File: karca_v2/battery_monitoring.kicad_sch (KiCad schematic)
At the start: 14 parts, among them U33 INA180A2, U34 MCP3204, U35 NUP4202, U36 TLV9301xDBV

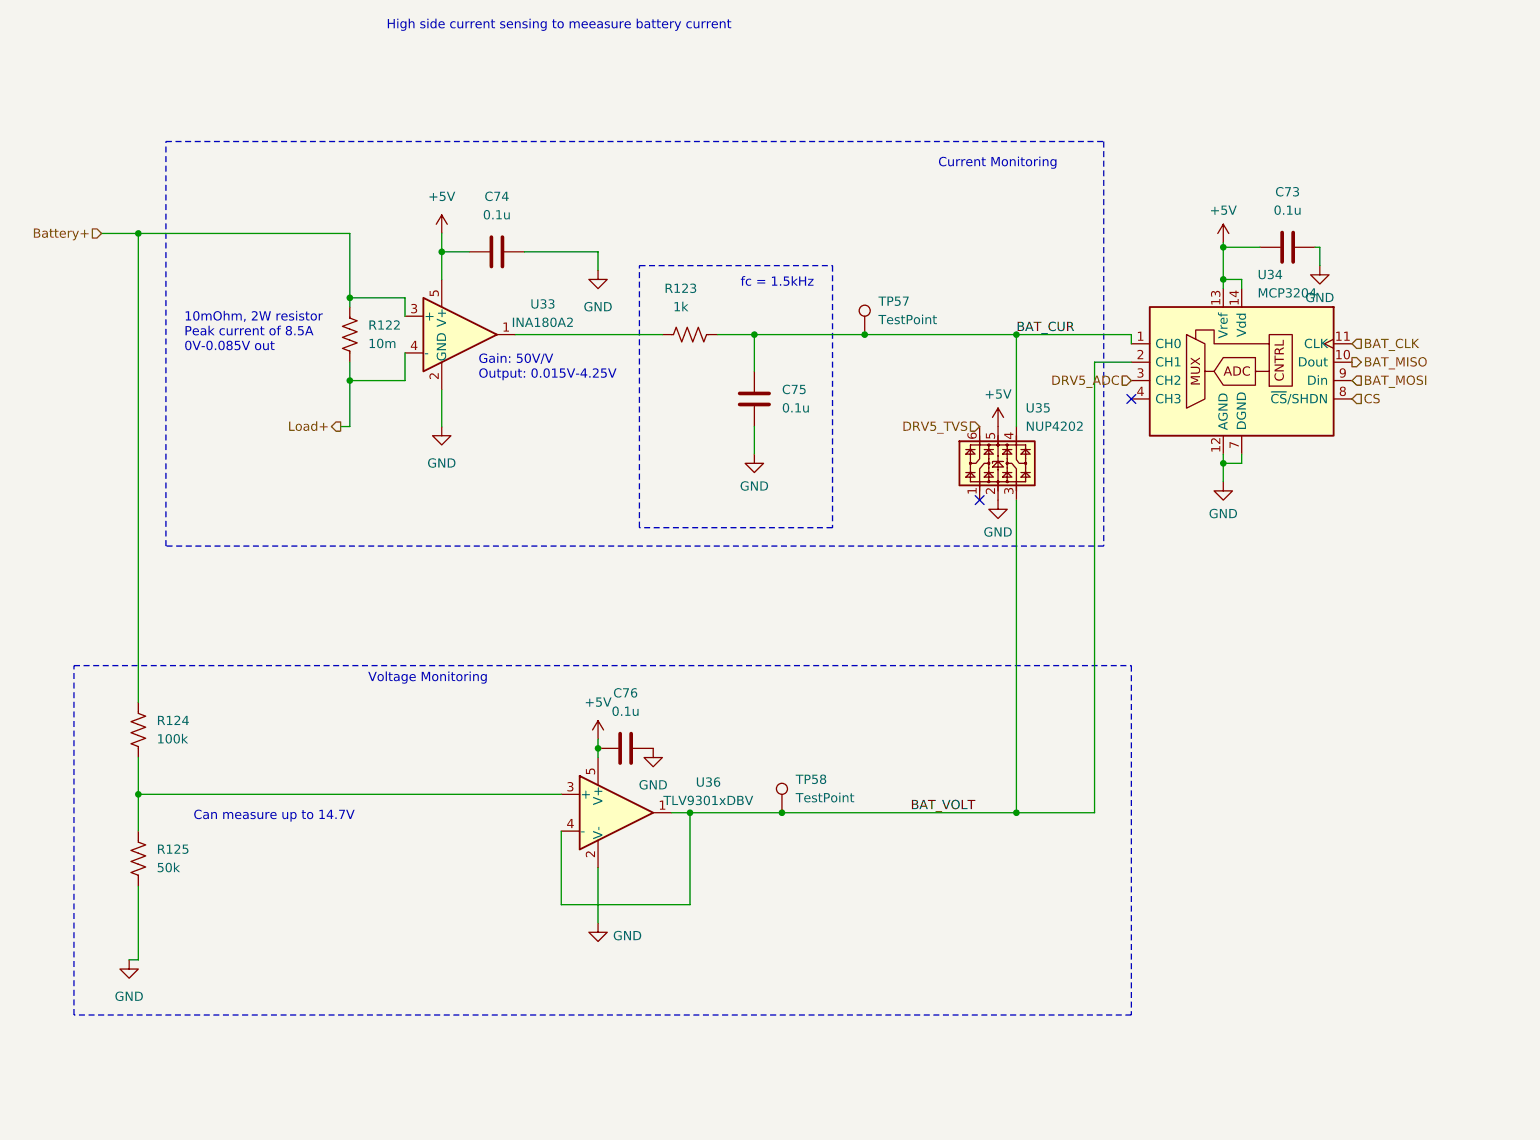
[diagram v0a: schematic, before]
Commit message: reorganized ADCs
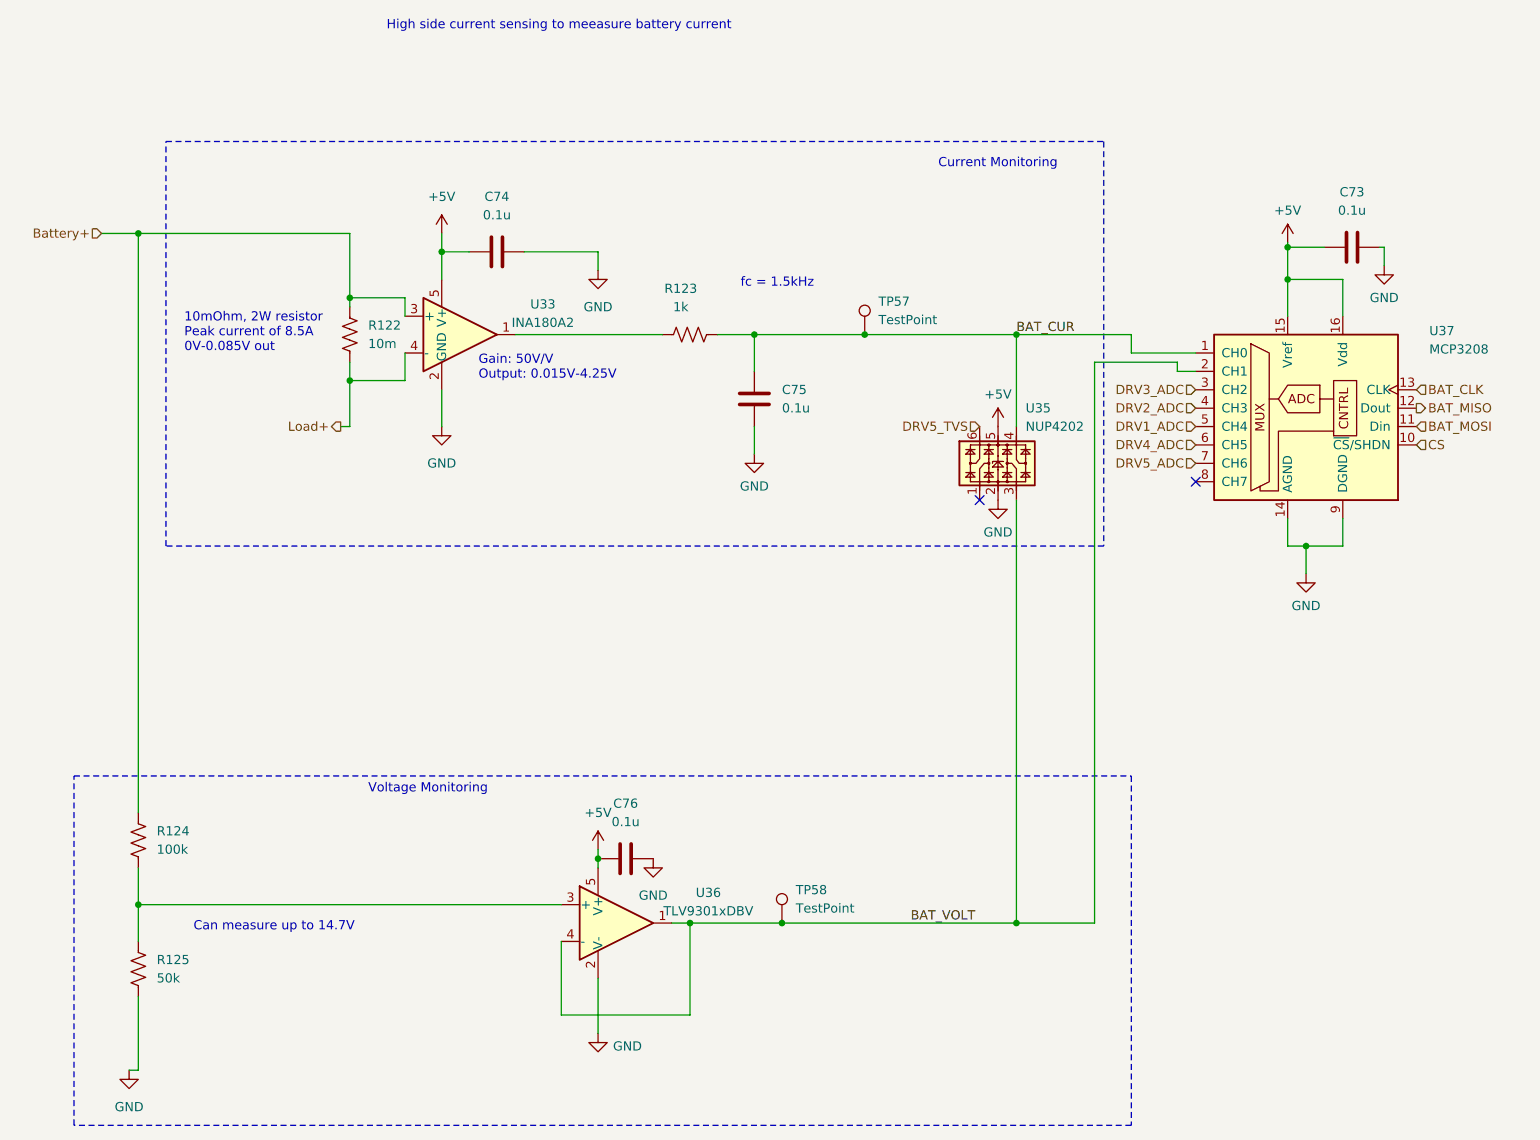
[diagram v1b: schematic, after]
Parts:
- removed U34: MCP3204, Package_SO:SO-14_3.9x8.65mm_P1.27mm, symbol Analog_ADC:MCP3204
- added U37: MCP3208, Package_SO:SOIC-16_3.9x9.9mm_P1.27mm, symbol Analog_ADC:MCP3208
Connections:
- net +5V: now also U37.15 (Vref), U37.16 (Vdd)
- net BAT_CLK: now also U37.13 (CLK)
- net BAT_CUR: now also U37.1 (CH0)
- net BAT_MISO: now also U37.12 (Dout)
- net BAT_MOSI: now also U37.11 (Din)
- net BAT_VOLT: now also U37.2 (CH1)
- net CS: now also U37.10 (~{CS}/SHDN)
- net DRV5_ADC: now also U37.7 (CH6)
- net GND: now also U37.14 (AGND), U37.9 (DGND)
- new net DRV1_ADC: U37.5 (CH4)
- new net DRV2_ADC: U37.4 (CH3)
- new net DRV3_ADC: U37.3 (CH2)
- new net DRV4_ADC: U37.6 (CH5)
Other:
- moved on the sheet: C73, C76, R124, R125, TP58, U36

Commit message: finished schematic for v2.1
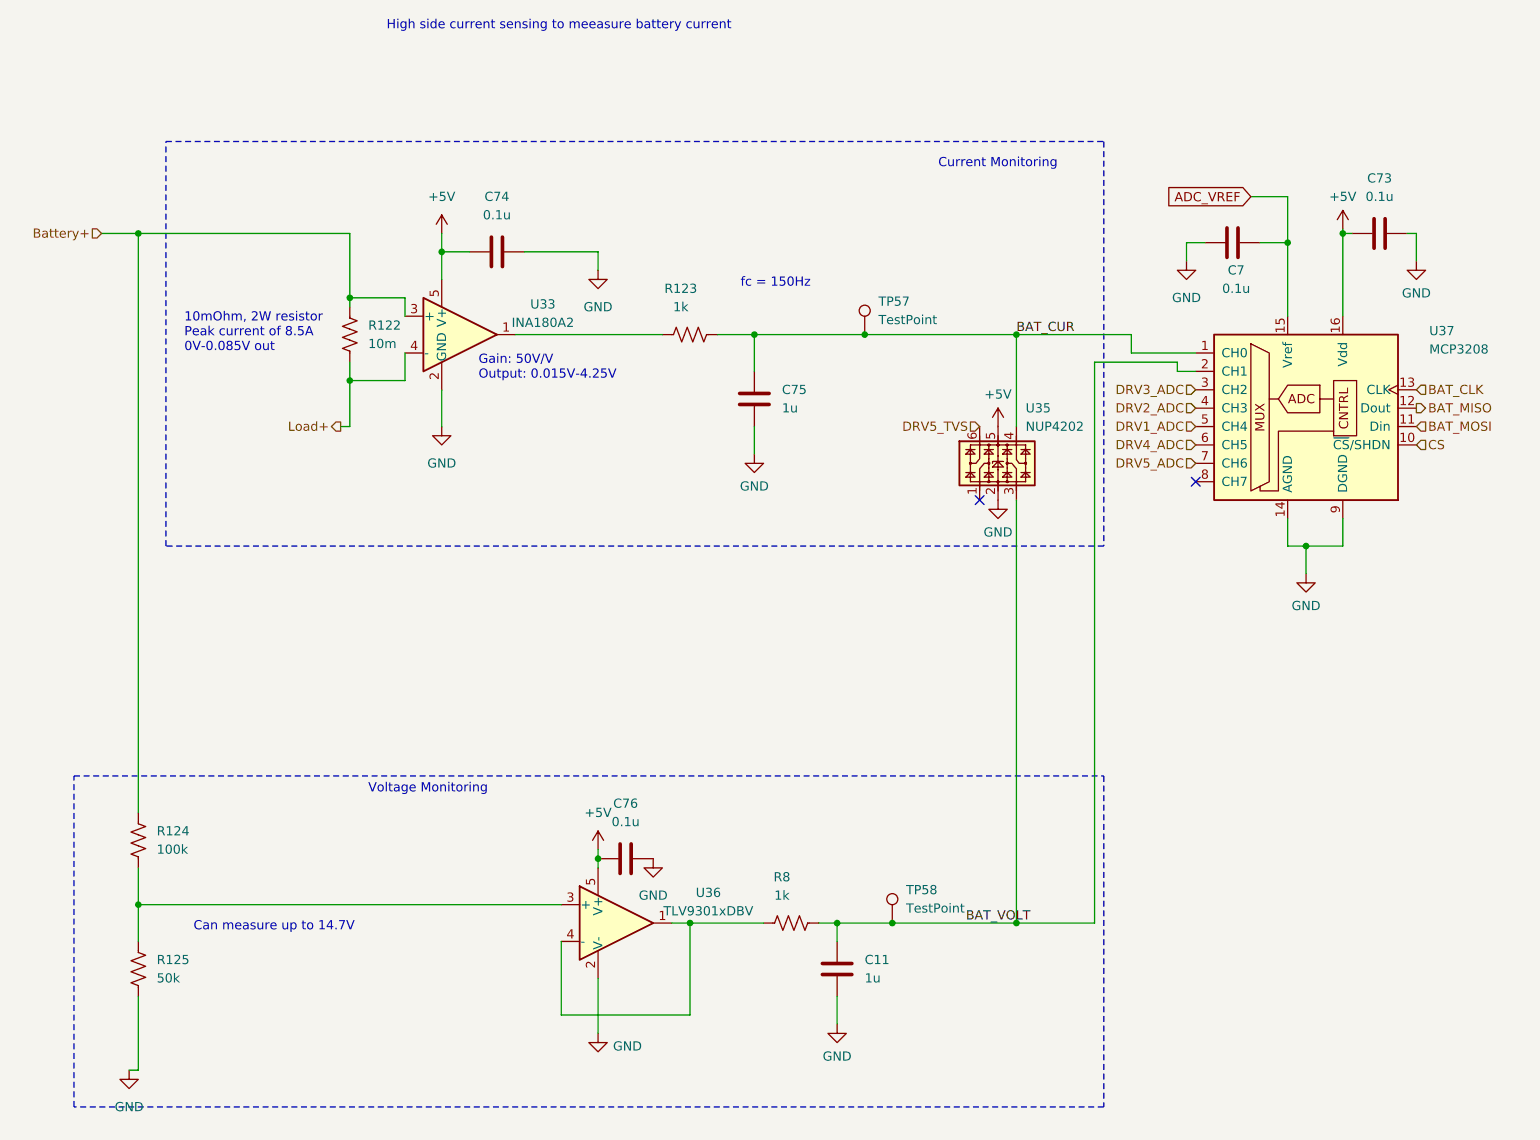
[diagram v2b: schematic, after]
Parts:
- added C11: 1u, Capacitor_SMD:C_1206_3216Metric, symbol Device:C
- added C7: 0.1u, Capacitor_SMD:C_1206_3216Metric, symbol Device:C
- added R8: 1k, Resistor_SMD:R_1206_3216Metric, symbol Device:R_US
- C75: value 0.1u -> 1u
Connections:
- net +5V: no longer U37.15 (Vref)
- net BAT_VOLT: now also C11.2, R8.2; no longer U36.1, U36.4 (-)
- net GND: now also C11.1, C7.1
- new net: R8.1, U36.1, U36.4 (-)
- new net ADC_VREF: C7.2, U37.15 (Vref)
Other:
- note added: "fc = 150Hz"
- note removed: "fc = 1.5kHz"
- moved on the sheet: C73, TP58

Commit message: swapped adcs
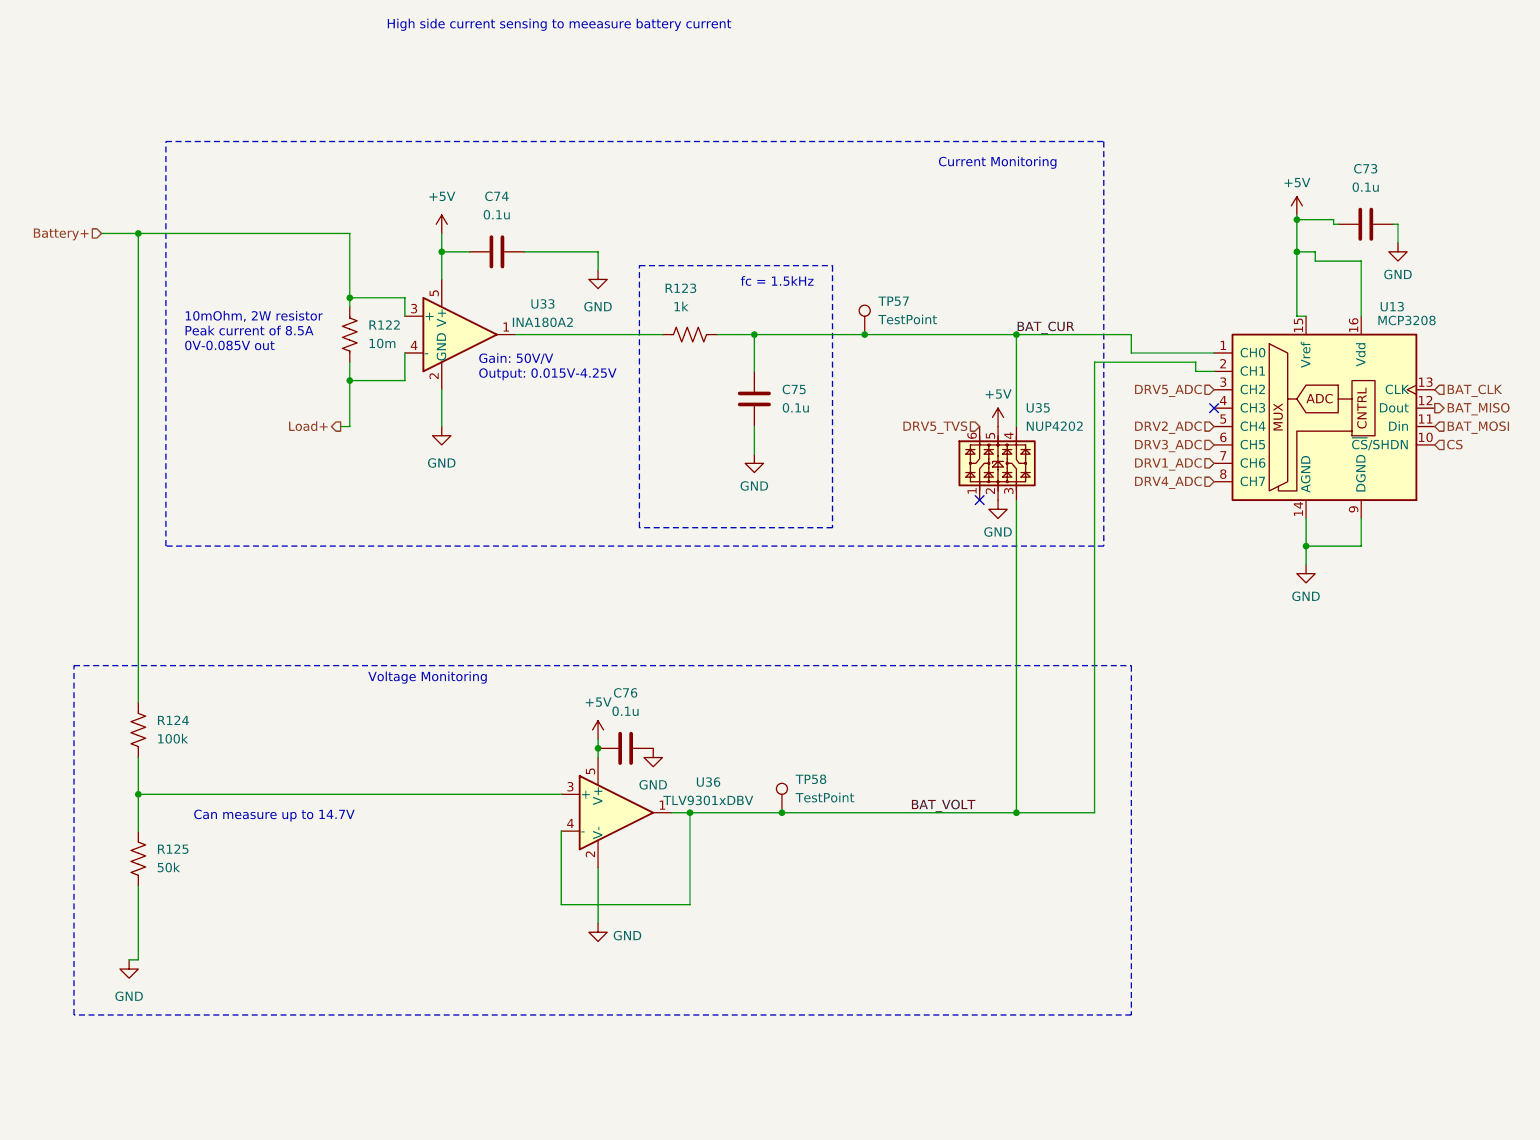
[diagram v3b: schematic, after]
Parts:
- removed C11: 1u, Capacitor_SMD:C_1206_3216Metric, symbol Device:C
- removed C7: 0.1u, Capacitor_SMD:C_1206_3216Metric, symbol Device:C
- removed R8: 1k, Resistor_SMD:R_1206_3216Metric, symbol Device:R_US
- removed U37: MCP3208, Package_SO:SOIC-16_3.9x9.9mm_P1.27mm, symbol Analog_ADC:MCP3208
- added U13: MCP3208, Package_SO:SOIC-16_3.9x9.9mm_P1.27mm, symbol Analog_ADC:MCP3208
- C75: value 1u -> 0.1u
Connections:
- net +5V: now also U13.15 (Vref), U13.16 (Vdd)
- net BAT_CLK: now also U13.13 (CLK)
- net BAT_CUR: now also U13.1 (CH0)
- net BAT_MISO: now also U13.12 (Dout)
- net BAT_MOSI: now also U13.11 (Din)
- net BAT_VOLT: now also U36.1, U36.4 (-), U13.2 (CH1)
- net CS: now also U13.10 (~{CS}/SHDN)
- net DRV1_ADC: now also U13.7 (CH6)
- net DRV2_ADC: now also U13.5 (CH4)
- net DRV3_ADC: now also U13.6 (CH5)
- net DRV4_ADC: now also U13.8 (CH7)
- net DRV5_ADC: now also U13.3 (CH2)
- net GND: now also U13.14 (AGND), U13.9 (DGND)
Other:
- note added: "fc = 1.5kHz"
- note removed: "fc = 150Hz"
- moved on the sheet: C73, C76, R124, R125, TP58, U36

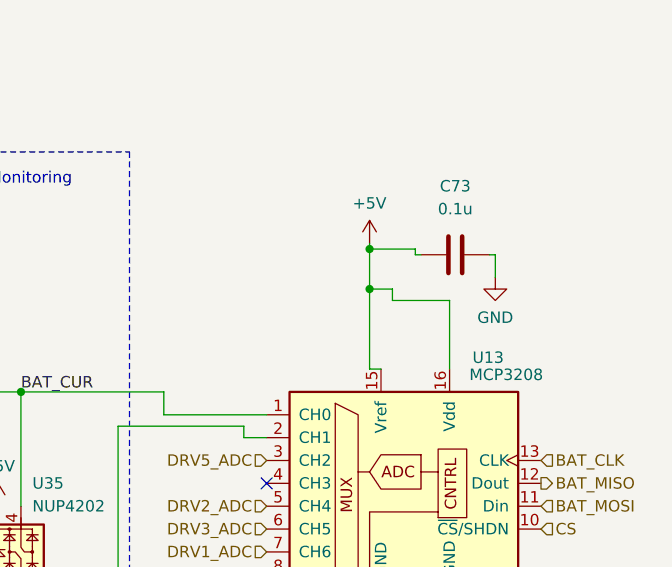
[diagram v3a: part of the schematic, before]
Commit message: added precision shunt reference to ADCs and second SPI bus for driver current and battery voltage monitors
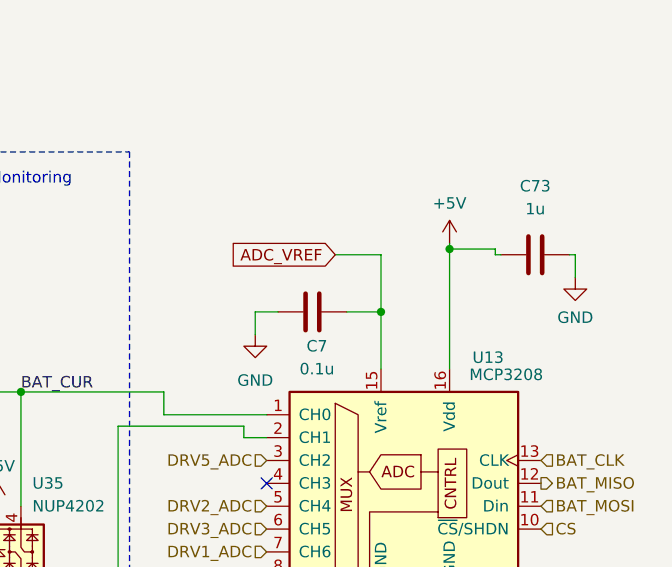
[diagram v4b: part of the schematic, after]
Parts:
- added C7: 0.1u, Capacitor_SMD:C_0805_2012Metric, symbol Device:C
- C73: value 0.1u -> 1u; footprint Capacitor_SMD:C_1206_3216Metric -> Capacitor_SMD:C_0805_2012Metric
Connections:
- net +5V: no longer U13.15 (Vref)
- net GND: now also C7.1
- new net ADC_VREF: C7.2, U13.15 (Vref)
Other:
- moved on the sheet: C73

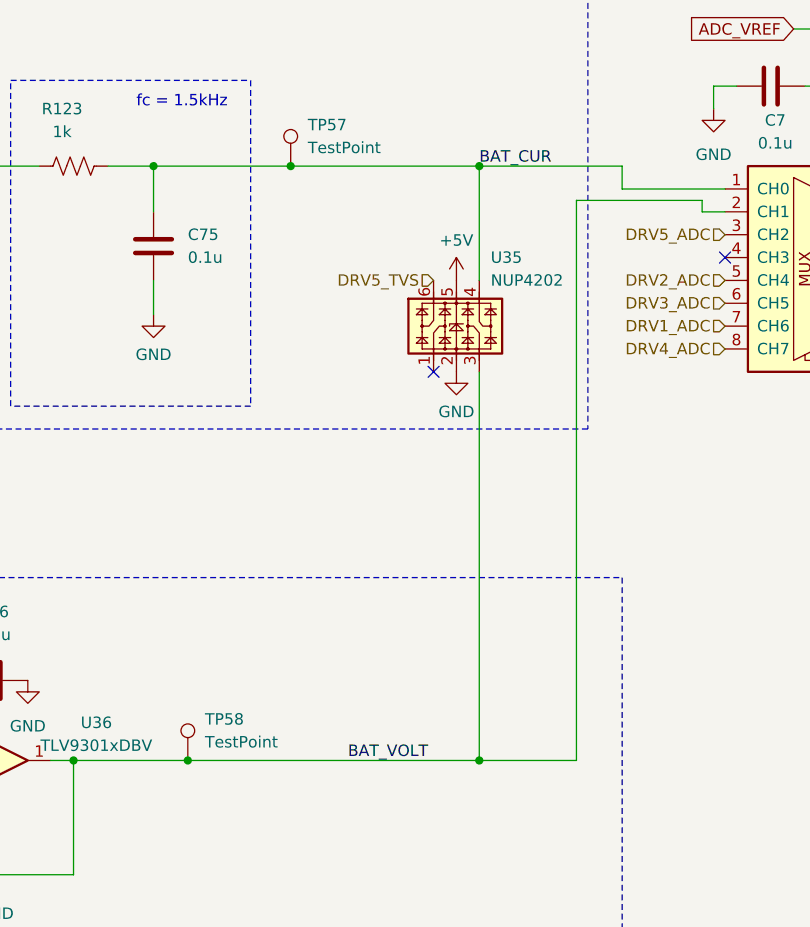
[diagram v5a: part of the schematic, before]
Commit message: fixed all routing. Now need to clean up vias
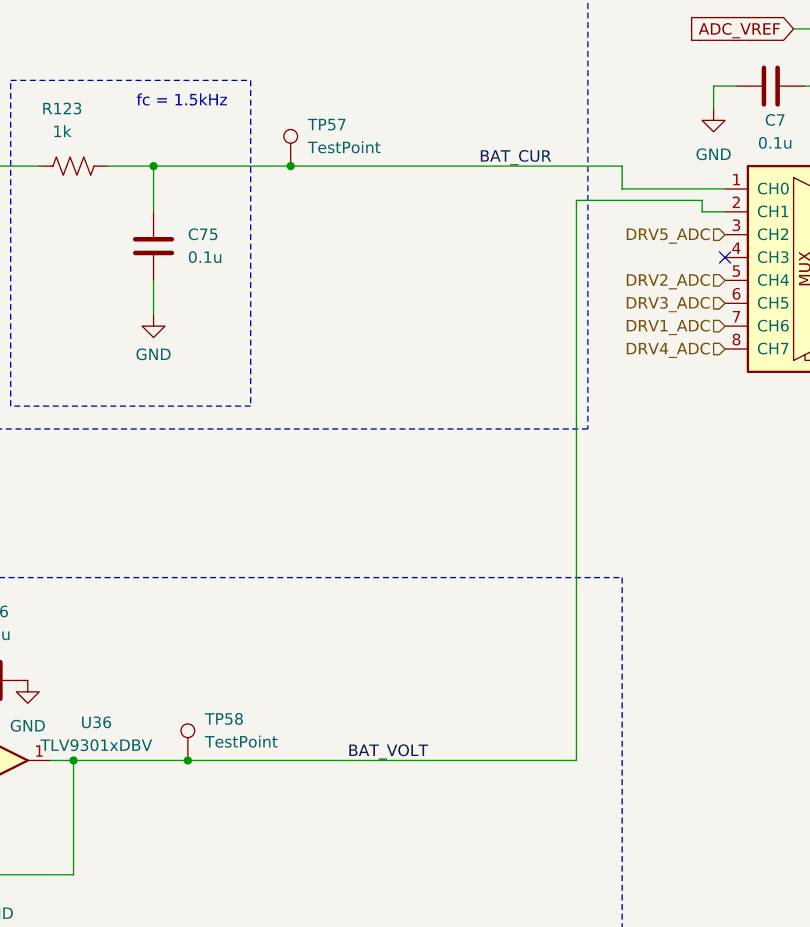
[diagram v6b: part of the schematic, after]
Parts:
- removed U35: NUP4202, Package_TO_SOT_SMD:SOT-363_SC-70-6, symbol Power_Protection:NUP4202
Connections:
- no-connect marks 2 -> 1
